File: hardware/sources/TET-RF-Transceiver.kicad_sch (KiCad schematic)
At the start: 28 parts, among them U11 SMA_1, U12 W25Q128JVSIQTR, U13 W25Q128JVSIQTR, U14 E80-900M2213S, U15 SMA_2, U16 W25Q128JVSIQTR, U17 TMP112AIDRLR, U18 INA226AQDGSRQ1, U19 TMP112AIDRLR

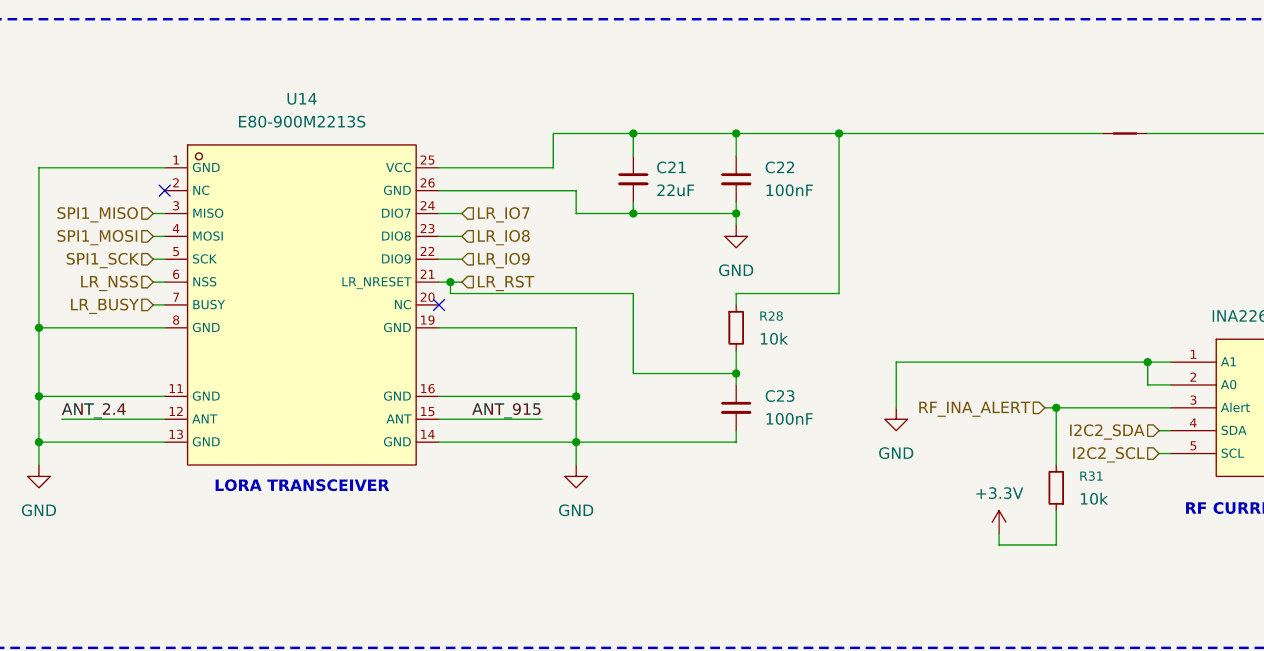
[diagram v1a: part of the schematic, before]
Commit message: hardware(schematic): fix Electrical Rules Check (ERC)
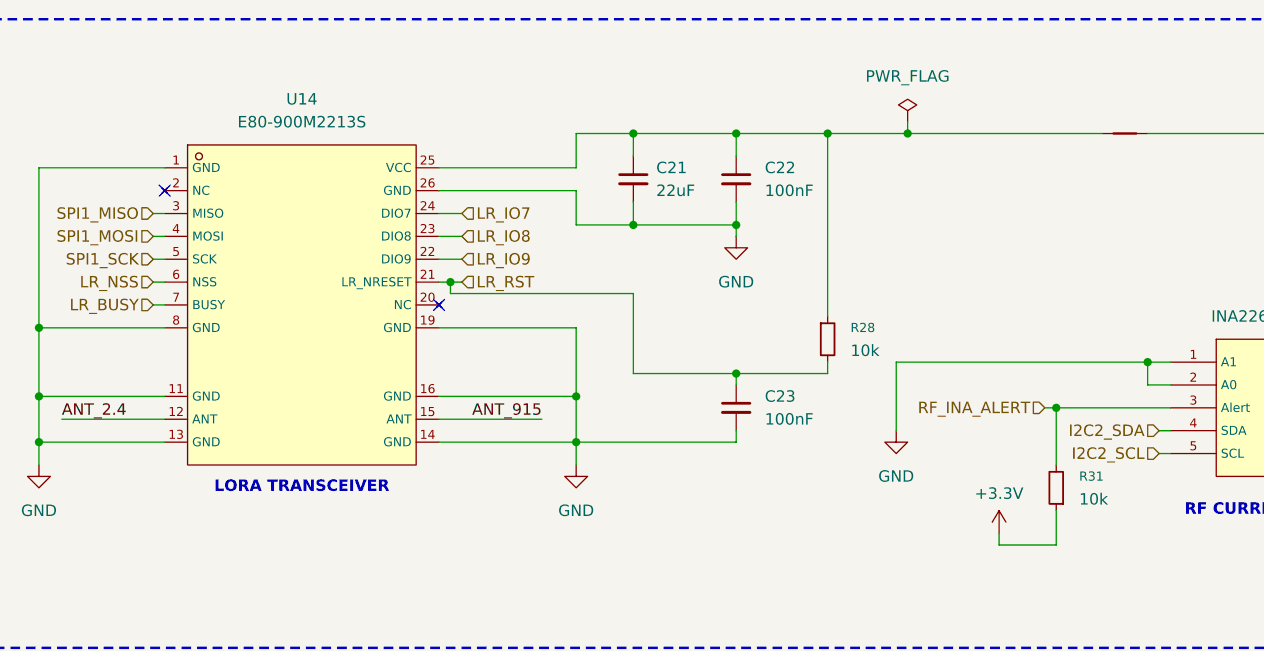
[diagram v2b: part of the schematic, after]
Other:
- moved on the sheet: R28

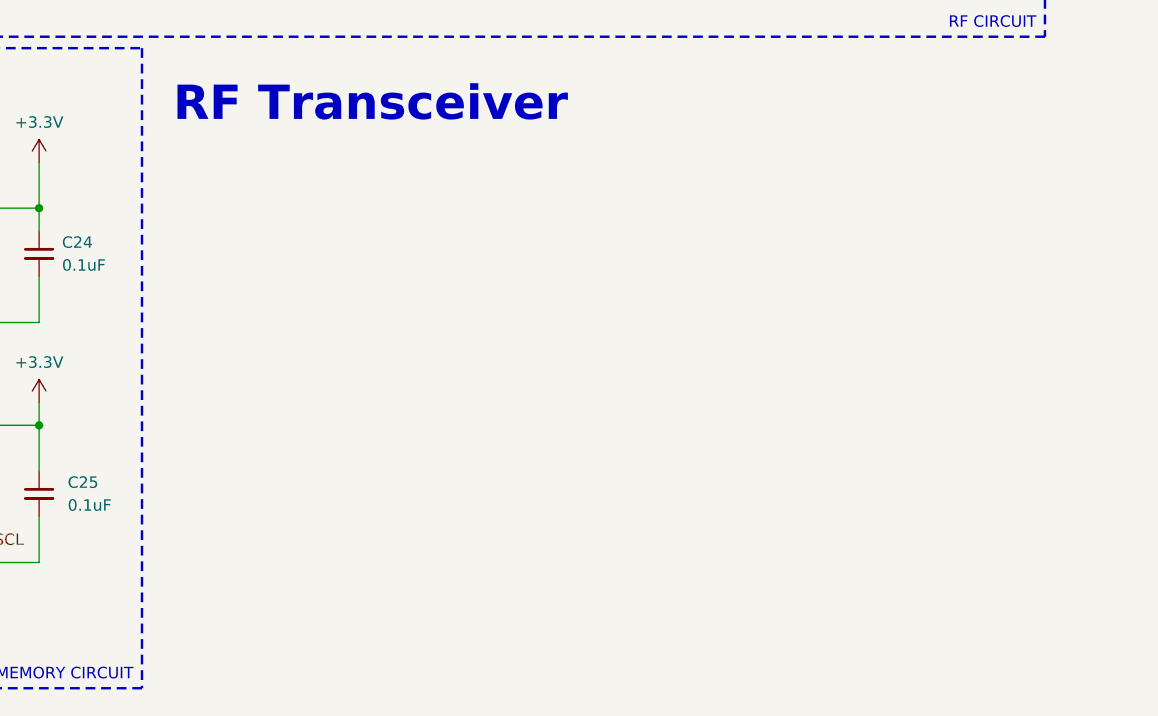
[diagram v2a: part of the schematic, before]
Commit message: hardware(schematic): update documentation for all sheets
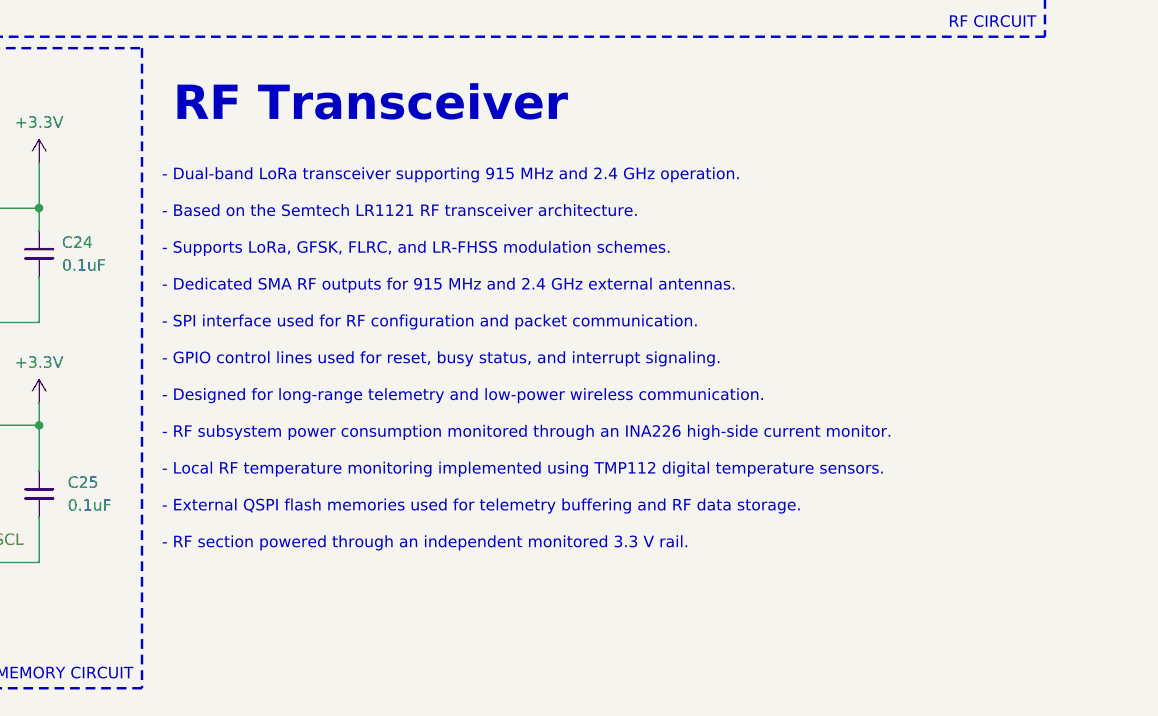
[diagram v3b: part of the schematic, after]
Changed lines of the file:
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@@
 		)
 	)
-	(text_box ""
+	(text_box "\n\n\n\n\n\n- Dual-band LoRa transceiver supporting 915 MHz and 2.4 GHz operation.\n\n- Based on the Semtech LR1121 RF transceiver architecture.\n\n- Supports LoRa, GFSK, FLRC, and LR-FHSS modulation schemes.\n\n- Dedicated SMA RF outputs for 915 MHz and 2.4 GHz external antennas.\n\n- SPI interface used for RF configuration and packet communication.\n\n- GPIO control lines used for reset, busy status, and interrupt signaling.\n\n- Designed for long-range telemetry and low-power wireless communication.\n\n- RF subsystem power consumption monitored through an INA226 high-side current monitor.\n\n- Local RF temperature monitoring implemented using TMP112 digital temperature sensors.\n\n- External QSPI flash memories used for telemetry buffering and RF data storage.\n\n- RF section powered through an independent monitored 3.3 V rail."
 		(exclude_from_sim no)
 		(at 184.15 85.09 0)

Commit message: hardware(pcb_design): start PCB design
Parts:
- removed NT3, NT4: NetTie_2, symbol Device:NetTie_2
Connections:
- net RF_SENSE- is gone; now on net +3.3V: R32.2, U18.8 (VBUS), U18.9 (VIN-)
- net RF_SENSE+: now also C21.1, C22.1, R28.1, U14.25 (VCC)
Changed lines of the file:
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@@
 	(wire
 		(pts
-			(xy 156.21 26.67) (xy 190.5 26.67)
-		)
-		(stroke
-			(width 0)
-			(type default)
-		)
-	)
-	(wire
-		(pts
 			(xy 22.86 116.84) (xy 22.86 115.57)
 		)
@@
 	(wire
 		(pts
-			(xy 129.54 26.67) (xy 151.13 26.67)
+			(xy 129.54 26.67) (xy 190.5 26.67)
 		)
 		(stroke
@@
 	(wire
 		(pts
-			(xy 201.93 26.67) (xy 236.22 26.67)
+			(xy 201.93 26.67) (xy 269.24 26.67)
 		)
 		(stroke
@@
 	(wire
 		(pts
-			(xy 241.3 26.67) (xy 269.24 26.67)
-		)
-		(stroke
-			(width 0)
-			(type default)
-		)
-	)
-	(wire
-		(pts
 			(xy 201.93 40.64) (xy 204.47 40.64)
 		)
@@
 	)
 	(symbol
-		(lib_id "Device:NetTie_2")
-		(at 238.76 26.67 0)
-		(unit 1)
-		(exclude_from_sim yes)
-		(in_bom no)
-		(on_board no)
-		(dnp no)
-		(fields_autoplaced yes)
-		(property "Reference" "NT4"
-			(at 238.76 21.59 0)
-			(effects
-				(font
-					(size 1.27 1.27)
-				)
-				(hide yes)
-			)
-		)
-		(property "Value" "NetTie_2"
-			(at 238.76 24.13 0)
-			(effects
-				(font
-					(size 1.27 1.27)
-				)
-				(hide yes)
-			)
-		)
-		(property "Footprint" ""
-			(at 238.76 26.67 0)
-			(effects
-				(font
-					(size 1.27 1.27)
-				)
-				(hide yes)
-			)
-		)
-		(property "Datasheet" "~"
-			(at 238.76 26.67 0)
-			(effects
-				(font
-					(size 1.27 1.27)
-				)
-				(hide yes)
-			)
-		)
-		(property "Description" "Net tie, 2 pins"
-			(at 238.76 26.67 0)
-			(effects
-				(font
-					(size 1.27 1.27)
-				)
-				(hide yes)
-			)
-		)
-		(pin "1"
-		)
-		(pin "2"
-		)
-		(instances
-			(project "TET"
-				(path "/9ad3bc3a-e567-4764-b6aa-630c8b7f3c7b/64ee994d-a0f8-4131-90b0-8a68ffe29a18"
-					(reference "NT4")
-					(unit 1)
-				)
-			)
-		)
-	)
-	(symbol
 		(lib_id "power:GND")
 		(at 161.29 144.78 0)
@@
 					(unit 1)
 				)
-			)
-		)
-	)
-	(symbol
-		(lib_id "Device:NetTie_2")
-		(at 153.67 26.67 0)
-		(unit 1)
-		(exclude_from_sim yes)
-		(in_bom no)
-		(on_board no)
-		(dnp no)
-		(fields_autoplaced yes)
-		(property "Reference" "NT3"
-			(at 153.67 21.59 0)
-			(effects
-				(font
-					(size 1.27 1.27)
-				)
-				(hide yes)
-			)
-		)
-		(property "Value" "NetTie_2"
-			(at 153.67 24.13 0)
-			(effects
-				(font
-					(size 1.27 1.27)
-				)
-				(hide yes)
-			)
-		)
-		(property "Footprint" ""
-			(at 153.67 26.67 0)
-			(effects
-				(font
-					(size 1.27 1.27)
-				)
-				(hide yes)
-			)
-		)
-		(property "Datasheet" "~"
-			(at 153.67 26.67 0)
-			(effects
-				(font
-					(size 1.27 1.27)
-				)
-				(hide yes)
-			)
-		)
-		(property "Description" "Net tie, 2 pins"
-			(at 153.67 26.67 0)
-			(effects
-				(font
-					(size 1.27 1.27)
-				)
-				(hide yes)
-			)
-		)
-		(pin "1"
-		)
-		(pin "2"
-		)
-		(instances
-			(project "TET"
-				(path "/9ad3bc3a-e567-4764-b6aa-630c8b7f3c7b/64ee994d-a0f8-4131-90b0-8a68ffe29a18"
-					(reference "NT3")
-					(unit 1)
-				)
